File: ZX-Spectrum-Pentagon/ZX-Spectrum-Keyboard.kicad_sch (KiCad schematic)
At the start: 131 parts, among them SW1 SW_Push_45deg, SW10 SW_Push_45deg, SW11 SW_Push_45deg, SW12 SW_Push_45deg, SW13 SW_Push_45deg, SW14 SW_Push_45deg, SW15 SW_Push_45deg, SW16 SW_Push_45deg, SW17 SW_Push_45deg, SW18 SW_Push_45deg, SW19 SW_Push_45deg, SW2 SW_Push_45deg, SW20 SW_Push_45deg, SW21 SW_Push_45deg, SW22 SW_Push_45deg, SW23 SW_Push_45deg, SW24 SW_Push_45deg, SW25 SW_Push_45deg, SW26 SW_Push_45deg, SW27 SW_Push_45deg, SW28 SW_Push_45deg, SW29 SW_Push_45deg, SW3 SW_Push_45deg, SW30 SW_Push_45deg, SW31 SW_Push_45deg, SW32 SW_Push_45deg, SW33 SW_Push_45deg, SW34 SW_Push_45deg, SW35 SW_Push_45deg, SW36 SW_Push_45deg, SW37 SW_Push_45deg, SW38 SW_Push_45deg, SW39 SW_Push_45deg, SW4 SW_Push_45deg, SW40 SW_Push_45deg, SW41 SW_Push_45deg, SW42 SW_Push_45deg, SW43 SW_Push_45deg, SW44 SW_Push_45deg, SW45 SW_Push_45deg, SW46 SW_Push_45deg, SW47 SW_Push_45deg, SW48 SW_Push_45deg, SW49 SW_Push_45deg, SW5 SW_Push_45deg, SW50 SW_Push_45deg, SW51 SW_Push_45deg, SW52 SW_Push_45deg, SW53 SW_Push_45deg, SW54 SW_Push_45deg, SW55 SW_Push_45deg, SW56 SW_Push_45deg, SW57 SW_Push_45deg, SW58 SW_Push_45deg, SW6 SW_Push_45deg, SW7 SW_Push_45deg, SW8 SW_Push_45deg, SW9 SW_Push_45deg, U1 74HC32, U2 74HC32, U3 74HC32, U4 74HC32, U5 74HC32

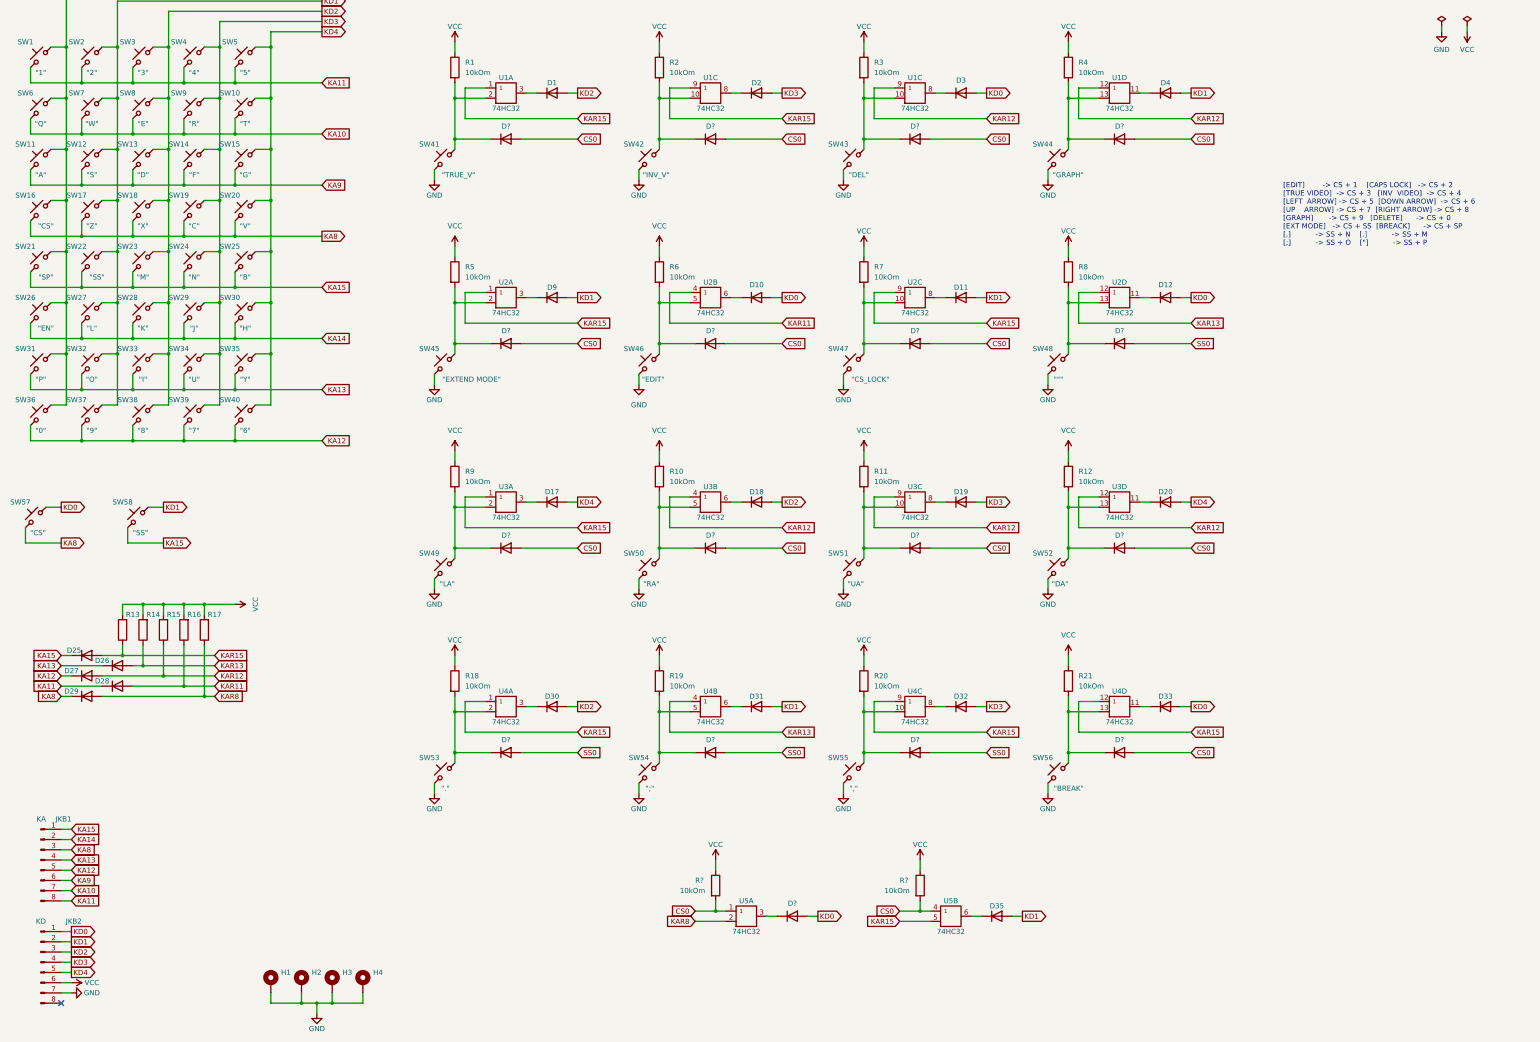
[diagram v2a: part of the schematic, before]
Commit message: add ket footprint library
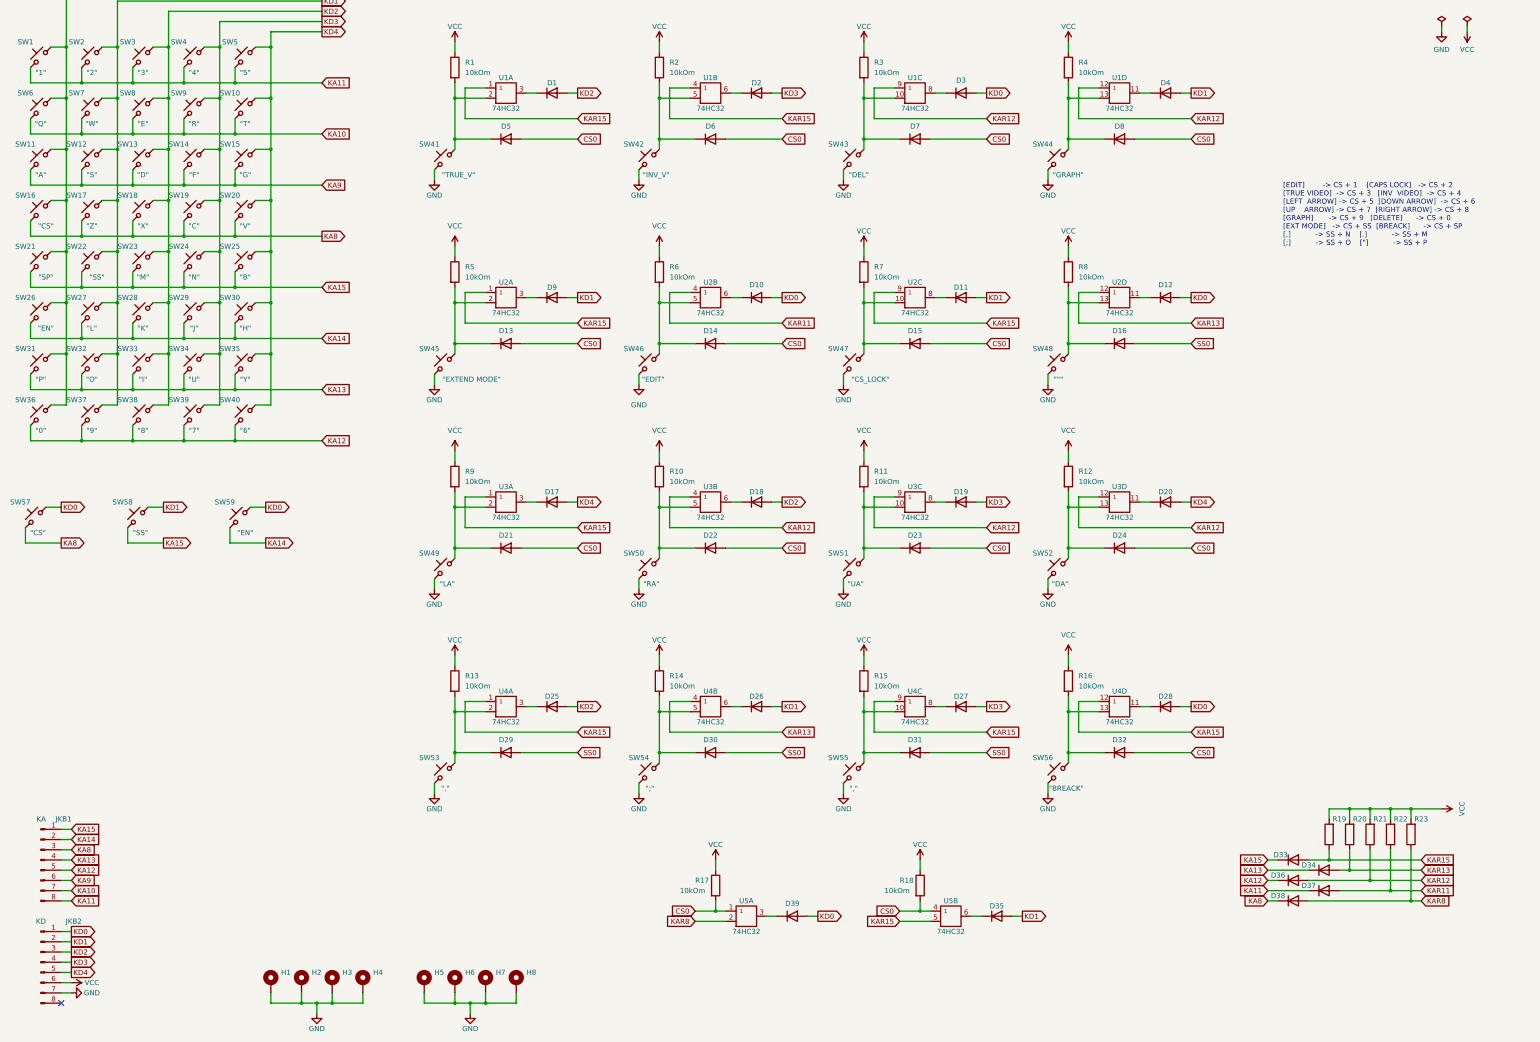
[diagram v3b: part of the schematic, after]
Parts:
- added H5, H6, H7, H8: MountingHole_Pad, MountingHole:MountingHole_2.5mm_Pad_Via, symbol Mechanical:MountingHole_Pad
- added SW59: SW_Push_45deg, Switch_Kailh_Cherry_MX_Universal:SW_Kailh_Cherry_MX_Universal_1.50u, symbol Switch:SW_Push_45deg
- SW1, SW10, SW11, SW12, SW13, SW14, SW15, SW17, SW18, SW19, SW2, SW20, SW23, SW24, SW25, SW27, SW28, SW29, SW3, SW30, SW31, SW32, SW33, SW34, SW35, SW36, SW37, SW38, SW39, SW4, SW40, SW41, SW42, SW44, SW46, SW47, SW49, SW5, SW50, SW51, SW52, SW58, SW6, SW7, SW8, SW9: footprint Button_Switch_Keyboard:SW_Cherry_MX_1.00u_PCB -> Switch_Kailh_Cherry_MX_Universal:SW_Kailh_Cherry_MX_Universal_1.00u
- SW16: footprint Button_Switch_Keyboard:SW_Cherry_MX_1.50u_PCB -> Switch_Kailh_Cherry_MX_Universal:SW_Kailh_Cherry_MX_Universal_2.00u
- SW21: footprint Button_Switch_Keyboard:SW_Cherry_MX_6.25u_PCB -> Switch_Kailh_Cherry_MX_Universal:SW_Kailh_Cherry_MX_Universal_6.25u
- SW22, SW48: footprint Button_Switch_Keyboard:SW_Cherry_MX_1.00u_PCB -> Switch_Kailh_Cherry_MX_Universal:SW_Kailh_Cherry_MX_Universal_1.25u
- SW26: footprint Button_Switch_Keyboard:SW_Cherry_MX_2.00u_PCB -> Switch_Kailh_Cherry_MX_Universal:SW_Kailh_Cherry_MX_Universal_2.25u
- SW43: footprint Button_Switch_Keyboard:SW_Cherry_MX_1.50u_PCB -> Switch_Kailh_Cherry_MX_Universal:SW_Kailh_Cherry_MX_Universal_1.50u
- SW45: footprint Button_Switch_Keyboard:SW_Cherry_MX_1.75u_PCB -> Switch_Kailh_Cherry_MX_Universal:SW_Kailh_Cherry_MX_Universal_1.75u
- SW53: footprint Button_Switch_Keyboard:SW_Cherry_MX_1.50u_PCB -> Switch_Kailh_Cherry_MX_Universal:SW_Kailh_Cherry_MX_Universal_1.00u
- SW54: footprint Button_Switch_Keyboard:SW_Cherry_MX_1.25u_PCB -> Switch_Kailh_Cherry_MX_Universal:SW_Kailh_Cherry_MX_Universal_1.25u
- SW55: footprint Button_Switch_Keyboard:SW_Cherry_MX_1.25u_PCB -> Switch_Kailh_Cherry_MX_Universal:SW_Kailh_Cherry_MX_Universal_1.00u
- SW56: footprint Button_Switch_Keyboard:SW_Cherry_MX_1.75u_PCB -> Switch_Kailh_Cherry_MX_Universal:SW_Kailh_Cherry_MX_Universal_2.00u; Name "BREAK" -> "BREACK"
- SW57: footprint Button_Switch_Keyboard:SW_Cherry_MX_2.00u_PCB -> Switch_Kailh_Cherry_MX_Universal:SW_Kailh_Cherry_MX_Universal_1.00u
- gave numbers to parts that had none: 19
- renumbered D30 to D25, D31 to D26, D32 to D27, D33 to D28, D25 to D33, D26 to D34, D27 to D36, D28 to D37, D29 to D38, R18 to R13, R19 to R14, R20 to R15, R21 to R16, R13 to R19, R14 to R20, R15 to R21, R16 to R22, R17 to R23
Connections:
- net GND: now also H5.1, H6.1, H7.1, H8.1
- net KA14: now also SW59.2
- net KAR15: now also U1.4 (A); no longer U1.9 (A)
- net KD0: now also SW59.1
- net at D6.2 (K), R2.2, SW42.1: now also U1.5 (B); no longer U1.10 (B)
- net at D2.2 (K): now also U1.6 (Y); no longer U1.8 (Y)
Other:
- moved on the sheet: D33, D34, D36, D37, D38, R19, R20, R21, R22, R23

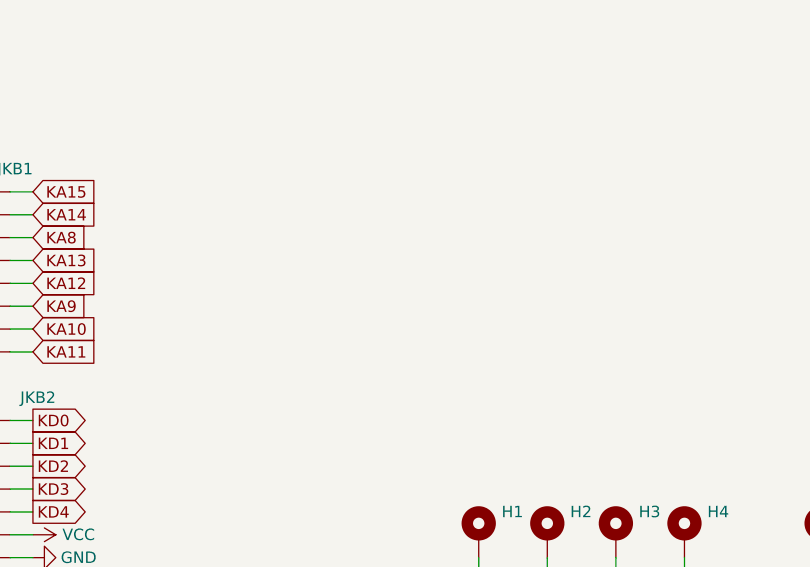
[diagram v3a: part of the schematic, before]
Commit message: reposition all button add stabilize
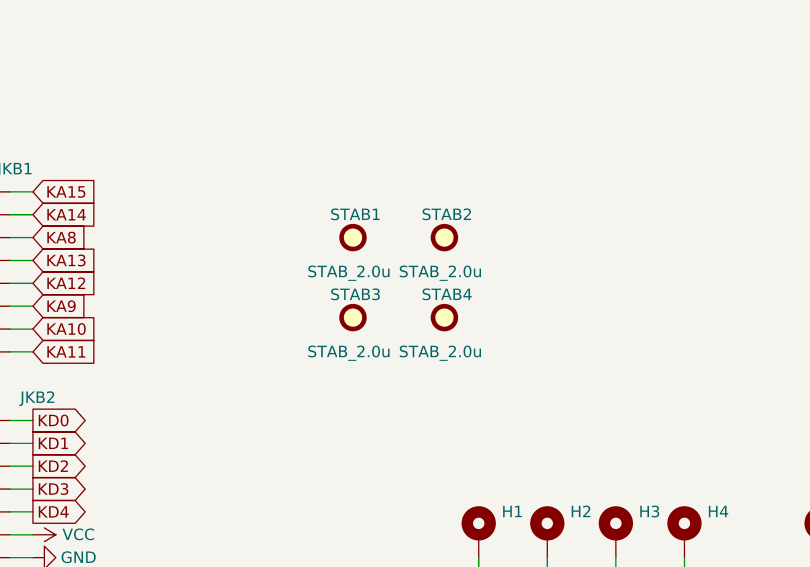
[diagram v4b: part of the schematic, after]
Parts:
- added STAB1, STAB2, STAB3: STAB_2.0u, Switch_Stabilizer:Stabilizer_Cherry_MX_2.00u, symbol Mechanical:Fiducial
- added STAB4: STAB_2.0u, Switch_Stabilizer:Stabilizer_Cherry_MX_6.25u, symbol Mechanical:Fiducial
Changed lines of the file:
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@@
     (pin "2")
   )
+  (symbol (lib_id "Mechanical:Fiducial") (at 86.36 228.6 0) (unit 1)
+    (in_bom yes) (on_board yes)
+    (property "Reference" "STAB2" (id 0) (at 83.82 226.06 0)
+      (effects (font (size 1.27 1.27)) (justify left))
+    )
+    (property "Value" "STAB_2.0u" (id 1) (at 81.28 232.41 0)
+      (effects (font (size 1.27 1.27)) (justify left))
+    )
+    (property "Footprint" "Switch_Stabilizer:Stabilizer_Cherry_MX_2.00u" (id 2) (at 86.36 228.6 0)
+      (effects (font (size 1.27 1.27)) hide)
+    )
+    (property "Datasheet" "~" (id 3) (at 86.36 228.6 0)
+      (effects (font (size 1.27 1.27)) hide)
+    )
+  )
   (symbol (lib_id "Simulation_SPICE:DIODE") (at 250.19 204.47 180) (unit 1)
     (in_bom yes) (on_board yes)
@@
     (pin "2")
   )
+  (symbol (lib_id "Mechanical:Fiducial") (at 76.2 228.6 0) (unit 1)
+    (in_bom yes) (on_board yes)
+    (property "Reference" "STAB1" (id 0) (at 73.66 226.06 0)
+      (effects (font (size 1.27 1.27)) (justify left))
+    )
+    (property "Value" "STAB_2.0u" (id 1) (at 71.12 232.41 0)
+      (effects (font (size 1.27 1.27)) (justify left))
+    )
+    (property "Footprint" "Switch_Stabilizer:Stabilizer_Cherry_MX_2.00u" (id 2) (at 76.2 228.6 0)
+      (effects (font (size 1.27 1.27)) hide)
+    )
+    (property "Datasheet" "~" (id 3) (at 76.2 228.6 0)
+      (effects (font (size 1.27 1.27)) hide)
+    )
+  )
   (symbol (lib_id "power:GND") (at 101.6 269.24 0) (unit 1)
     (in_bom yes) (on_board yes)
@@
     (pin "1")
   )
+  (symbol (lib_id "Mechanical:Fiducial") (at 86.36 237.49 0) (unit 1)
+    (in_bom yes) (on_board yes)
+    (property "Reference" "STAB4" (id 0) (at 83.82 234.95 0)
+      (effects (font (size 1.27 1.27)) (justify left))
+    )
+    (property "Value" "STAB_2.0u" (id 1) (at 81.28 241.3 0)
+      (effects (font (size 1.27 1.27)) (justify left))
+    )
+    (property "Footprint" "Switch_Stabilizer:Stabilizer_Cherry_MX_6.25u" (id 2) (at 86.36 237.49 0)
+      (effects (font (size 1.27 1.27)) hide)
+    )
+    (property "Datasheet" "~" (id 3) (at 86.36 237.49 0)
+      (effects (font (size 1.27 1.27)) hide)
+    )
+  )
+  (symbol (lib_id "Mechanical:Fiducial") (at 76.2 237.49 0) (unit 1)
+    (in_bom yes) (on_board yes)
+    (property "Reference" "STAB3" (id 0) (at 73.66 234.95 0)
+      (effects (font (size 1.27 1.27)) (justify left))
+    )
+    (property "Value" "STAB_2.0u" (id 1) (at 71.12 241.3 0)
+      (effects (font (size 1.27 1.27)) (justify left))
+    )
+    (property "Footprint" "Switch_Stabilizer:Stabilizer_Cherry_MX_2.00u" (id 2) (at 76.2 237.49 0)
+      (effects (font (size 1.27 1.27)) hide)
+    )
+    (property "Datasheet" "~" (id 3) (at 76.2 237.49 0)
+      (effects (font (size 1.27 1.27)) hide)
+    )
+  )
   (symbol (lib_id "Switch:SW_Push_45deg") (at 83.82 107.95 0) (mirror y) (unit 1)
     (in_bom yes) (on_board yes)
@@
       (reference "R23") (unit 1) (value "10kOm") (footprint "Resistor_SMD:R_0805_2012Metric_Pad1.20x1.40mm_HandSolder")
     )
+    (path "/09240150-163c-4e40-8bd8-2e2b627feda7"
+      (reference "STAB1") (unit 1) (value "STAB_2.0u") (footprint "Switch_Stabilizer:Stabilizer_Cherry_MX_2.00u")
+    )
+    (path "/01e8167f-028d-496a-8315-eadbf74acf2e"
+      (reference "STAB2") (unit 1) (value "STAB_2.0u") (footprint "Switch_Stabilizer:Stabilizer_Cherry_MX_2.00u")
+    )
+    (path "/13e478ab-2e0e-4d38-a56d-c180f4fadf5e"
+      (reference "STAB3") (unit 1) (value "STAB_2.0u") (footprint "Switch_Stabilizer:Stabilizer_Cherry_MX_2.00u")
+    )
+    (path "/12cac08a-1860-4331-bb92-2d93390df838"
+      (reference "STAB4") (unit 1) (value "STAB_2.0u") (footprint "Switch_Stabilizer:Stabilizer_Cherry_MX_6.25u")
+    )
     (path "/193fffdb-6d57-4615-912b-d47027430963"

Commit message: Trace route
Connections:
- net KAR12: now also U1.12 (A), U1.9 (A); no longer U1.12 (A), U1.9 (A)
- net at D8.2 (K), R4.2, SW44.1: now also U1.10 (B); no longer U1.13 (B)
- net at D4.2 (K): now also U1.8 (Y); no longer U1.11 (Y)
- net at D7.2 (K), R3.2, SW43.1: now also U1.13 (B); no longer U1.10 (B)
- net at D3.2 (K): now also U1.11 (Y); no longer U1.8 (Y)
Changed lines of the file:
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@@
     (pin "2")
   )
-  (symbol (lib_id "74IEC:74HC32") (at 250.19 40.64 0) (unit 3)
+  (symbol (lib_id "74IEC:74HC32") (at 250.19 40.64 0) (unit 4)
     (in_bom yes) (on_board yes)
     (property "Reference" "U1" (id 0) (at 250.19 36.83 0))
@@
     (pin "2")
   )
-  (symbol (lib_id "74IEC:74HC32") (at 300.99 40.64 0) (unit 4)
+  (symbol (lib_id "74IEC:74HC32") (at 300.99 40.64 0) (unit 3)
     (in_bom yes) (on_board yes)
     (property "Reference" "U1" (id 0) (at 300.99 36.83 0))
@@
       (reference "U1") (unit 2) (value "74HC32") (footprint "Package_SO:SOIC-14_3.9x8.7mm_P1.27mm")
     )
-    (path "/218985be-ffec-440b-a96d-a24f8531e9d3"
+    (path "/e0f11823-9813-47d2-917a-2d296488de25"
       (reference "U1") (unit 3) (value "74HC32") (footprint "Package_SO:SOIC-14_3.9x8.7mm_P1.27mm")
     )
-    (path "/e0f11823-9813-47d2-917a-2d296488de25"
+    (path "/218985be-ffec-440b-a96d-a24f8531e9d3"
       (reference "U1") (unit 4) (value "74HC32") (footprint "Package_SO:SOIC-14_3.9x8.7mm_P1.27mm")
     )

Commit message: trace route ZX-keyboard
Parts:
- added unit 4 of U5
- added unit 3 of U5
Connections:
- net CS0: no longer R18.2, U5.4 (A)
- net GND: now also U5.7 (GND), U5.7 (GND)
- net KAR11: now also U2.9 (A); no longer U2.4 (A)
- net KAR15: now also U2.4 (A); no longer U2.9 (A)
- net SS0: now also R18.2, U5.4 (A)
- net VCC: now also U5.14 (VCC), U5.14 (VCC)
- net at D15.2 (K), R7.2, SW47.1: now also U2.5 (B); no longer U2.10 (B)
- net at D14.2 (K), R6.2, SW46.1: now also U2.10 (B); no longer U2.5 (B)
- net at D10.2 (K): now also U2.8 (Y); no longer U2.6 (Y)
- net at D11.2 (K): now also U2.6 (Y); no longer U2.8 (Y)
- no-connect marks 1 -> 7
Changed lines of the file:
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@@
   (junction (at 237.49 41.91) (diameter 0) (color 0 0 0 0)
   )
+  (no_connect (at 229.87 260.35))
   (no_connect (at 38.1 266.7))
+  (no_connect (at 240.03 261.62))
+  (no_connect (at 203.2 260.35))
+  (no_connect (at 229.87 262.89))
+  (no_connect (at 213.36 261.62))
+  (no_connect (at 203.2 262.89))
   (wire (pts (xy 35.56 54.61) (xy 39.37 54.61))
     (stroke (width 0) (type default) (color 0 0 0 0))
@@
     )
   )
-  (global_label "CS0" (shape input) (at 246.38 243.84 180) (fields_autoplaced)
+  (global_label "SS0" (shape input) (at 246.38 243.84 180) (fields_autoplaced)
     (effects (font (size 1.27 1.27)) (justify right))
-    (property "Intersheet References" "${INTERSHEET_REFS}" (id 0) (at 240.3668 243.7606 0)
+    (property "Intersheet References" "${INTERSHEET_REFS}" (id 0) (at 240.4272 243.7606 0)
       (effects (font (size 1.27 1.27)) (justify right) hide)
     )
@@
     (pin "2")
   )
+  (symbol (lib_id "74IEC:74HC32") (at 234.95 261.62 0) (unit 4)
+    (in_bom yes) (on_board yes)
+    (property "Reference" "U5" (id 0) (at 234.95 257.81 0))
+    (property "Value" "74HC32" (id 1) (at 234.95 265.43 0))
+    (property "Footprint" "Package_SO:SOIC-14_3.9x8.7mm_P1.27mm" (id 2) (at 234.95 269.24 0)
+      (effects (font (size 1.27 1.27)) hide)
+    )
+    (property "Datasheet" "https://www.ti.com/lit/ug/scyd013b/scyd013b.pdf" (id 3) (at 234.95 257.81 0)
+      (effects (font (size 1.27 1.27)) hide)
+    )
+    (pin "14")
+    (pin "7")
+    (pin "1")
+    (pin "2")
+    (pin "3")
+    (pin "4")
+    (pin "5")
+    (pin "6")
+    (pin "10")
+    (pin "8")
+    (pin "9")
+    (pin "11")
+    (pin "12")
+    (pin "13")
+  )
   (symbol (lib_id "power:VCC") (at 251.46 231.14 0) (unit 1)
     (in_bom yes) (on_board yes)
@@
     (pin "13")
   )
-  (symbol (lib_id "74IEC:74HC32") (at 199.39 91.44 0) (unit 2)
+  (symbol (lib_id "74IEC:74HC32") (at 199.39 91.44 0) (unit 3)
     (in_bom yes) (on_board yes)
     (property "Reference" "U2" (id 0) (at 199.39 87.63 0))
@@
     (pin "2")
   )
+  (symbol (lib_id "74IEC:74HC32") (at 208.28 261.62 0) (unit 3)
+    (in_bom yes) (on_board yes)
+    (property "Reference" "U5" (id 0) (at 208.28 257.81 0))
+    (property "Value" "74HC32" (id 1) (at 208.28 265.43 0))
+    (property "Footprint" "Package_SO:SOIC-14_3.9x8.7mm_P1.27mm" (id 2) (at 208.28 269.24 0)
+      (effects (font (size 1.27 1.27)) hide)
+    )
+    (property "Datasheet" "https://www.ti.com/lit/ug/scyd013b/scyd013b.pdf" (id 3) (at 208.28 257.81 0)
+      (effects (font (size 1.27 1.27)) hide)
+    )
+    (pin "14")
+    (pin "7")
+    (pin "1")
+    (pin "2")
+    (pin "3")
+    (pin "4")
+    (pin "5")
+    (pin "6")
+    (pin "10")
+    (pin "8")
+    (pin "9")
+    (pin "11")
+    (pin "12")
+    (pin "13")
+  )
   (symbol (lib_id "Simulation_SPICE:DIODE") (at 270.51 245.11 180) (unit 1)
     (in_bom yes) (on_board yes)
@@
     (pin "2")
   )
-  (symbol (lib_id "74IEC:74HC32") (at 250.19 91.44 0) (unit 3)
+  (symbol (lib_id "74IEC:74HC32") (at 250.19 91.44 0) (unit 2)
     (in_bom yes) (on_board yes)
     (property "Reference" "U2" (id 0) (at 250.19 87.63 0))
@@
       (reference "U2") (unit 1) (value "74HC32") (footprint "Package_SO:SOIC-14_3.9x8.7mm_P1.27mm")
     )
-    (path "/5a9c2a1a-53d8-4a1e-b7b6-200d7e161f10"
+    (path "/d5de425e-dd2b-44fa-8358-ad5ec62f7f70"
       (reference "U2") (unit 2) (value "74HC32") (footprint "Package_SO:SOIC-14_3.9x8.7mm_P1.27mm")
     )
-    (path "/d5de425e-dd2b-44fa-8358-ad5ec62f7f70"
+    (path "/5a9c2a1a-53d8-4a1e-b7b6-200d7e161f10"
       (reference "U2") (unit 3) (value "74HC32") (footprint "Package_SO:SOIC-14_3.9x8.7mm_P1.27mm")
     )
@@
       (reference "U5") (unit 2) (value "74HC32") (footprint "Package_SO:SOIC-14_3.9x8.7mm_P1.27mm")
     )
+    (path "/9c396a39-4df8-48de-9da1-7f74962be36f"
+      (reference "U5") (unit 3) (value "74HC32") (footprint "Package_SO:SOIC-14_3.9x8.7mm_P1.27mm")
+    )
+    (path "/4b958b44-ceaa-4bc0-82ab-5a4c545742a5"
+      (reference "U5") (unit 4) (value "74HC32") (footprint "Package_SO:SOIC-14_3.9x8.7mm_P1.27mm")
+    )
   )
